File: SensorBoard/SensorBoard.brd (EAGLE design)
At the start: 134.6 x 100 mm, 70 parts, among them IC1 7805, J1 DCJ0202, U1 MPU-6000QFN-24, X1 gen1, X13 3.3out1, X14 3.3out2, X15 uart1, X16 uart2, X17 uart3, X18 uart4, X2 motordriver1, X3 MINI-USB-SCHIELD-32005-201, X4 gen2, X5 gen3, X6 gen4, X8 motordriver2

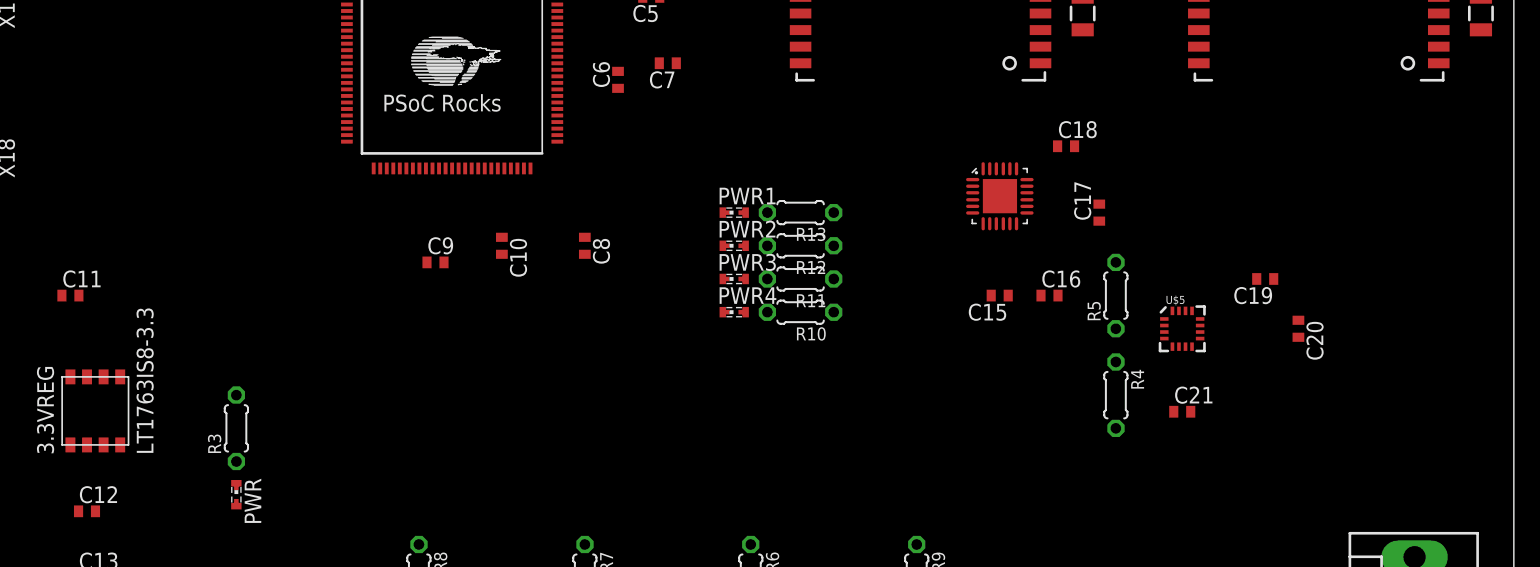
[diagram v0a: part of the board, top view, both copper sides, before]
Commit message: finished schematic.  All that is left is routing...
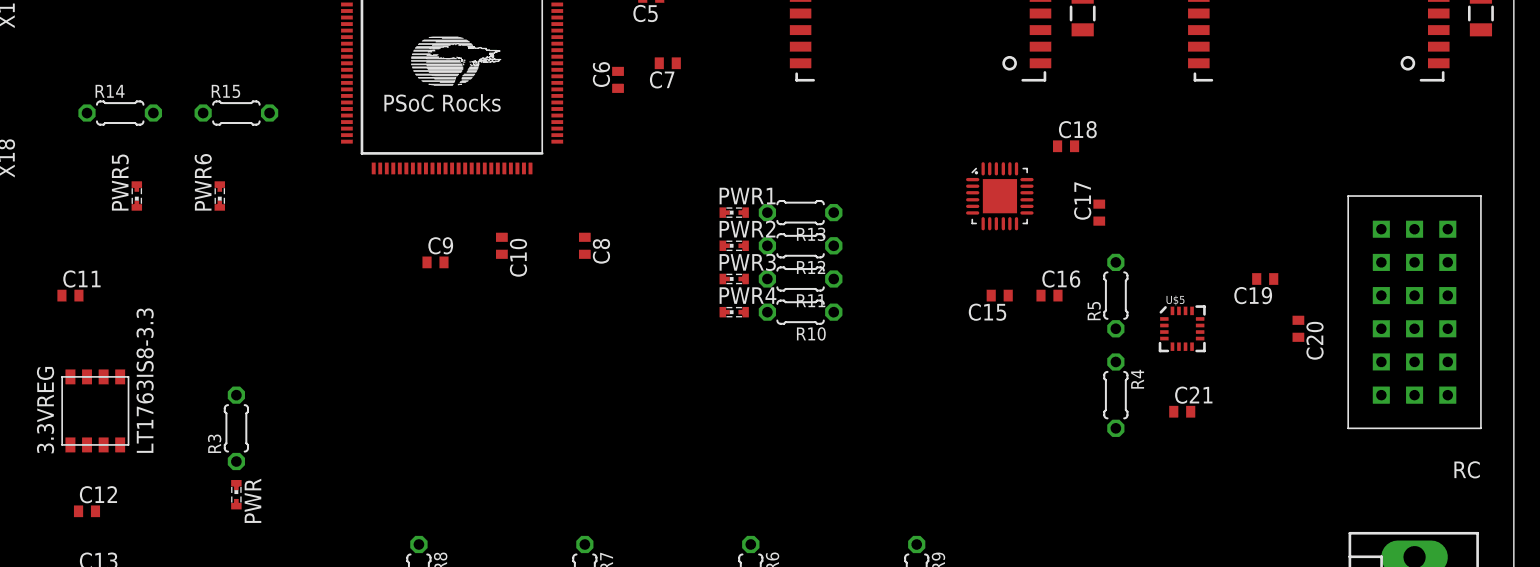
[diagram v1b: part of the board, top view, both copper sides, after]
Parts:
- added PWR5: GREEN, led:SMARTLED-TTW
- added PWR6: RED, led:SMARTLED-TTW
- added R14, R15: 4k, resistor:0204/5
- added RC: 6-CHANNEL, RCRECIEVER:6-CHANNEL
- C14: value 0.33uF -> 100nF
- X7: value (none) -> programmer
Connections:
- new net CH1: CY8C5868AXI-LP035.42, RC.P$3
- new net CH2: CY8C5868AXI-LP035.43, RC.P$6
- new net CH3: CY8C5868AXI-LP035.44, RC.P$9
- new net CH4: CY8C5868AXI-LP035.47, RC.P$12
- new net CH5: CY8C5868AXI-LP035.48, RC.P$15
- new net CH6: CY8C5868AXI-LP035.49, RC.P$18
- new net N$20: PWR5.A@1, R14.1
- new net N$21: PWR6.A@1, R15.1
- net +5V: now also RC.P$11, RC.P$14, RC.P$17, RC.P$2, RC.P$5, RC.P$8
- net CTS#: now also CY8C5868AXI-LP035.36
- net GND: now also PWR5.C@1, PWR6.C@1, RC.P$1, RC.P$10, RC.P$13, RC.P$16, RC.P$4, RC.P$7
- net RTS#: now also CY8C5868AXI-LP035.35
- net RXLED: now also R15.2
- net TXLED: now also R14.2
- net USB_RXD: now also CY8C5868AXI-LP035.27
- net USB_TXD: now also CY8C5868AXI-LP035.28

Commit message: fished SensorBoard.  It is perrrfect! - jack
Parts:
- removed U$5: HMC5883LSMD, SparkFun-Sensors:16LPCC
- removed U1: MPU-6000QFN-24, SparkFun-Sensors:QFN-24-TESTING
- removed X3: MINI-USB-SCHIELD-32005-201, con-cypressindustries:32005-201
- added ACC: MPU-6000QFN-24, SparkFun-Sensors:QFN-24-TESTING
- added MAGNETO: HMC5883LSMD, SparkFun-Sensors:16LPCC
- added MINIUSB: MINI-USB-SCHIELD-32005-201, con-cypressindustries:32005-201
- moved U$2 129.3 mm to (3.00, 92.0), turned to 0 degrees
- moved X15 112.2 mm to (122.0, 92.0), turned to 0 degrees
- moved X16 112.2 mm to (122.0, 80.0), turned to 0 degrees
- moved X17 112.1 mm to (122.0, 68.0), turned to 0 degrees
- moved X18 112.1 mm to (122.0, 56.0), turned to 0 degrees
- moved U$4 104.4 mm to (32.0, 92.0), turned to 0 degrees
- moved U$1 99.6 mm to (3.00, 70.0), turned to 0 degrees
- moved GPS2 87.0 mm to (25.0, 96.0), turned to 270 degrees
- moved C19 78.9 mm to (39.0, 23.0), turned to 0 degrees
- moved C20 77.4 mm to (42.0, 24.0)
- moved C14 77.3 mm to (100.0, 82.0), turned to 90 degrees
- moved USBUART 75.6 mm to (108.1, 77.9)
- moved R2 71.7 mm to (91.0, 83.0), turned to 0 degrees
- moved U$3 70.0 mm to (32.0, 70.0), turned to 0 degrees
- moved R1 69.7 mm to (97.0, 86.0), turned to 90 degrees
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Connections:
- new net +3.3VP1: PI.1
- new net +3.3VP2: PI.17
- new net +5VP1: PI.2
- new net +5VP2: PI.4
- new net 1: CY8C5868AXI-LP035.90
- new net 2: CY8C5868AXI-LP035.89
- new net 3: CY8C5868AXI-LP035.80
- new net 37: CY8C5868AXI-LP035.49
- new net 44: CY8C5868AXI-LP035.67
- net +3.3V: now also ACC.13, ACC.8, MAGNETO.13, MAGNETO.2, MAGNETO.4; no longer PI.1, PI.17, U$5.13, U$5.2, U$5.4, U1.13, U1.8
- net +5V: no longer PI.2, PI.4
- net AUXCL1: now also ACC.7, MAGNETO.1; no longer U$5.1, U1.7
- net AUXDA1: now also ACC.6, MAGNETO.16; no longer U$5.16, U1.6
- net CH1: now also CY8C5868AXI-LP035.51; no longer CY8C5868AXI-LP035.42
- net CH2: now also CY8C5868AXI-LP035.52; no longer CY8C5868AXI-LP035.43
- net CH3: now also CY8C5868AXI-LP035.53; no longer CY8C5868AXI-LP035.44
- net CH4: now also CY8C5868AXI-LP035.54; no longer CY8C5868AXI-LP035.47
- net CH5: now also CY8C5868AXI-LP035.55; no longer CY8C5868AXI-LP035.48
- net CH6: now also CY8C5868AXI-LP035.56; no longer CY8C5868AXI-LP035.49
- net CLKOUT1: now also ACC.22; no longer U1.22
- net CTS#: now also CY8C5868AXI-LP035.70; no longer CY8C5868AXI-LP035.36
- net D+: now also MINIUSB.3; no longer X3.3
- net D-: now also MINIUSB.2; no longer X3.2
- net FSYNC: now also ACC.11; no longer U1.11
- net GEN1: now also CY8C5868AXI-LP035.30; no longer CY8C5868AXI-LP035.31
- net GEN2: now also CY8C5868AXI-LP035.31; no longer CY8C5868AXI-LP035.32
- net GEN3: now also CY8C5868AXI-LP035.32; no longer CY8C5868AXI-LP035.33
- net GEN4: now also CY8C5868AXI-LP035.33; no longer CY8C5868AXI-LP035.34
- net GEN5: now also CY8C5868AXI-LP035.28; no longer CY8C5868AXI-LP035.29
- net GEN6: now also CY8C5868AXI-LP035.29; no longer CY8C5868AXI-LP035.30
- net GND: now also ACC.1, ACC.18, ACC.9, MAGNETO.11, MAGNETO.9, MINIUSB.1; no longer U$5.11, U$5.9, U1.1, U1.18, U1.9, X3.1
- net GPIO10: now also CY8C5868AXI-LP035.85; no longer CY8C5868AXI-LP035.82
- net GPIO11: now also CY8C5868AXI-LP035.83; no longer CY8C5868AXI-LP035.80
- net GPIO14: now also CY8C5868AXI-LP035.82; no longer CY8C5868AXI-LP035.1
- net GPIO15: now also CY8C5868AXI-LP035.81; no longer CY8C5868AXI-LP035.2
- net GPIO17: now also CY8C5868AXI-LP035.91; no longer CY8C5868AXI-LP035.85
- net GPIO18: no longer CY8C5868AXI-LP035.3
- net GPIO2(0): now also CY8C5868AXI-LP035.94; no longer CY8C5868AXI-LP035.91
- net GPIO22: no longer CY8C5868AXI-LP035.83
- net GPIO23: now also CY8C5868AXI-LP035.79; no longer CY8C5868AXI-LP035.16
- net GPIO24: now also CY8C5868AXI-LP035.78; no longer CY8C5868AXI-LP035.17
- net GPIO25: no longer CY8C5868AXI-LP035.18
- net GPIO27: no longer CY8C5868AXI-LP035.84
- net GPIO3(1): now also CY8C5868AXI-LP035.93; no longer CY8C5868AXI-LP035.90
- net GPIO4: now also CY8C5868AXI-LP035.92; no longer CY8C5868AXI-LP035.89
- net GPIO7: no longer CY8C5868AXI-LP035.52
- net GPIO8: no longer CY8C5868AXI-LP035.19
- net GPIO9: now also CY8C5868AXI-LP035.84; no longer CY8C5868AXI-LP035.81
- net GPS1RXA: now also CY8C5868AXI-LP035.19; no longer CY8C5868AXI-LP035.7
- net GPS1RXB: now also CY8C5868AXI-LP035.22; no longer CY8C5868AXI-LP035.9
- net GPS1TXA: now also CY8C5868AXI-LP035.17; no longer CY8C5868AXI-LP035.6
- net GPS1TXB: now also CY8C5868AXI-LP035.18; no longer CY8C5868AXI-LP035.8
- net GPS1XSTB: now also CY8C5868AXI-LP035.23; no longer CY8C5868AXI-LP035.22
- net GPS2RXA: now also CY8C5868AXI-LP035.3; no longer CY8C5868AXI-LP035.98
- net GPS2RXB: now also CY8C5868AXI-LP035.4; no longer CY8C5868AXI-LP035.96
- net GPS2TXA: now also CY8C5868AXI-LP035.1; no longer CY8C5868AXI-LP035.99
- net GPS2TXB: now also CY8C5868AXI-LP035.2; no longer CY8C5868AXI-LP035.97
- net GPS2XSTB: now also CY8C5868AXI-LP035.5; no longer CY8C5868AXI-LP035.23
- net GPS3RXA: now also CY8C5868AXI-LP035.8; no longer CY8C5868AXI-LP035.94
- net GPS3RXB: now also CY8C5868AXI-LP035.9; no longer CY8C5868AXI-LP035.92
- net GPS3TXA: now also CY8C5868AXI-LP035.6; no longer CY8C5868AXI-LP035.95
- net GPS3TXB: now also CY8C5868AXI-LP035.7; no longer CY8C5868AXI-LP035.93
- net GPS3XSTB: now also CY8C5868AXI-LP035.16; no longer CY8C5868AXI-LP035.24
- net GPS4RXA: now also CY8C5868AXI-LP035.97; no longer CY8C5868AXI-LP035.78
- net GPS4RXB: now also CY8C5868AXI-LP035.98; no longer CY8C5868AXI-LP035.76
- net GPS4TXA: now also CY8C5868AXI-LP035.95; no longer CY8C5868AXI-LP035.79
- net GPS4TXB: now also CY8C5868AXI-LP035.96; no longer CY8C5868AXI-LP035.77
- net GPS4XSTB: now also CY8C5868AXI-LP035.99; no longer CY8C5868AXI-LP035.25
- net INT1: now also ACC.12, CY8C5868AXI-LP035.27; no longer U1.12
- net MDTX1: now also CY8C5868AXI-LP035.34; no longer CY8C5868AXI-LP035.46
- net MDTX2: now also CY8C5868AXI-LP035.35; no longer CY8C5868AXI-LP035.45
- net N$11: now also MAGNETO.12; no longer U$5.12
- net N$15: now also MAGNETO.8; no longer U$5.8
- net N$16: now also MAGNETO.10; no longer U$5.10
- net N$6: now also MINIUSB.4, MINIUSB.5; no longer X3.4, X3.5
- net N$7: now also ACC.10; no longer U1.10
- net N$8: now also ACC.20; no longer U1.20
- net PWREN#: now also CY8C5868AXI-LP035.74
- net RTS#: now also CY8C5868AXI-LP035.71; no longer CY8C5868AXI-LP035.35
- net RX1: now also CY8C5868AXI-LP035.77; no longer CY8C5868AXI-LP035.74
- net RX2: now also CY8C5868AXI-LP035.69; no longer CY8C5868AXI-LP035.72
- net RX3: now also CY8C5868AXI-LP035.48; no longer CY8C5868AXI-LP035.70
- net RX4: now also CY8C5868AXI-LP035.46; no longer CY8C5868AXI-LP035.68
- net SCL_ACC: now also ACC.23, CY8C5868AXI-LP035.25; no longer CY8C5868AXI-LP035.4, U1.23
- net SDA_ACC: now also ACC.24, CY8C5868AXI-LP035.24; no longer CY8C5868AXI-LP035.5, U1.24
- net STATUS1: now also CY8C5868AXI-LP035.44; no longer CY8C5868AXI-LP035.56
- net STATUS2: now also CY8C5868AXI-LP035.43; no longer CY8C5868AXI-LP035.55
- net STATUS3: now also CY8C5868AXI-LP035.42; no longer CY8C5868AXI-LP035.54
- net STATUS4: now also CY8C5868AXI-LP035.36; no longer CY8C5868AXI-LP035.53
- net TX1: now also CY8C5868AXI-LP035.76; no longer CY8C5868AXI-LP035.73
- net TX2: now also CY8C5868AXI-LP035.68; no longer CY8C5868AXI-LP035.71
- net TX3: now also CY8C5868AXI-LP035.47; no longer CY8C5868AXI-LP035.69
- net TX4: now also CY8C5868AXI-LP035.45; no longer CY8C5868AXI-LP035.67
- net USB_RXD: now also CY8C5868AXI-LP035.73; no longer CY8C5868AXI-LP035.27
- net USB_TXD: now also CY8C5868AXI-LP035.72; no longer CY8C5868AXI-LP035.28
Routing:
- net +5V: track 0.00 -> 475.9 mm, vias 0 -> 5
- net GND: track 0.00 -> 371.4 mm, vias 0 -> 18
- net +3.3V: track 0.00 -> 247.9 mm, vias 0 -> 4
- net XRES: track 0.00 -> 101.4 mm, vias 0 -> 2
- net SCLK: track 0.00 -> 89.9 mm
- net SDAT: track 0.00 -> 86.3 mm, vias 0 -> 2
- net MDTX2: track 0.00 -> 71.3 mm, vias 0 -> 2
- net GEN5: track 0.00 -> 64.4 mm, vias 0 -> 2
- net MDTX1: track 0.00 -> 62.4 mm, vias 0 -> 2
- net TX3: track 0.00 -> 61.6 mm, vias 0 -> 1
- net GPS2TXA: track 0.00 -> 61.0 mm, vias 0 -> 2
- net GPS2TXB: track 0.00 -> 60.0 mm, vias 0 -> 2
- net GPS2RXA: track 0.00 -> 58.9 mm, vias 0 -> 2
- net GPS2RXB: track 0.00 -> 57.6 mm, vias 0 -> 2
- net GPS1RXB: track 0.00 -> 56.9 mm, vias 0 -> 2
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- added copper zone on layer 1, net GND
- added copper zone on layer 16, net GND
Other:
- board size 134.6 x 100 mm -> 136.2 x 101 mm

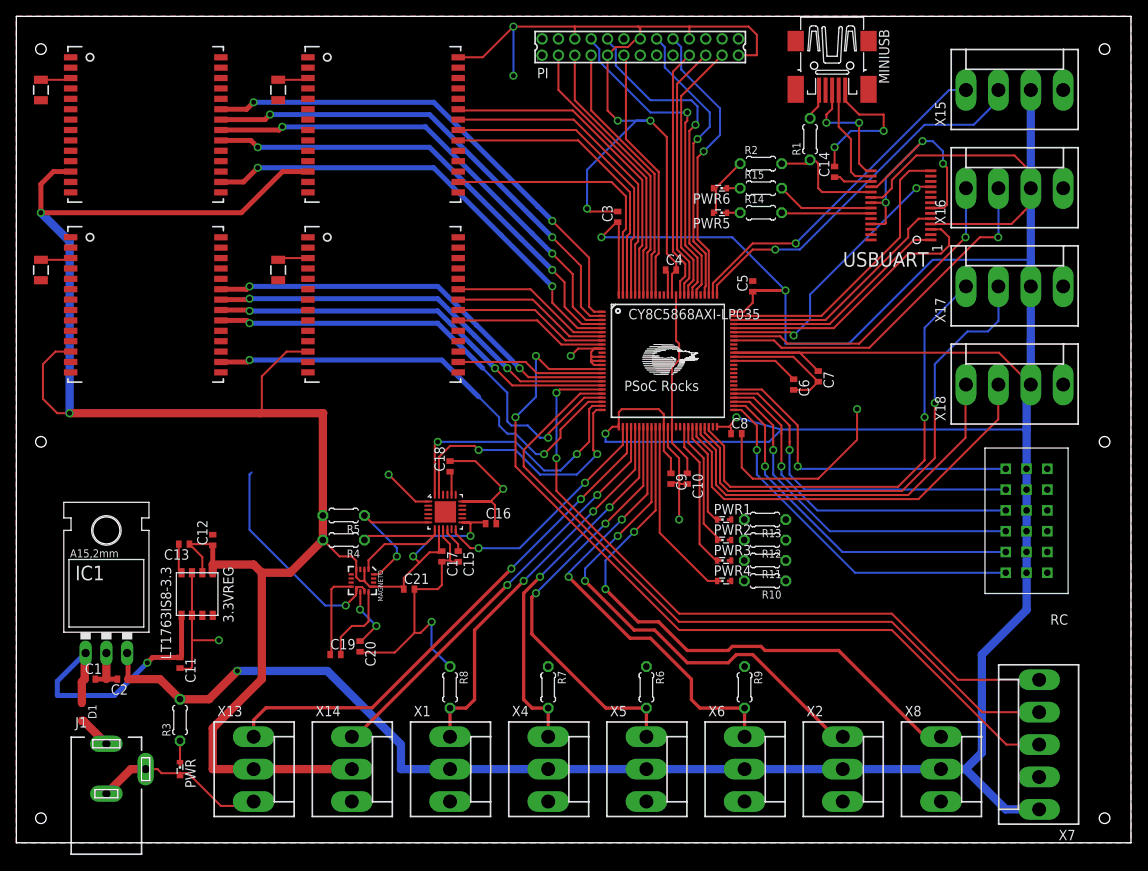
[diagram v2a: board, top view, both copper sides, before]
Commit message: added screw holes
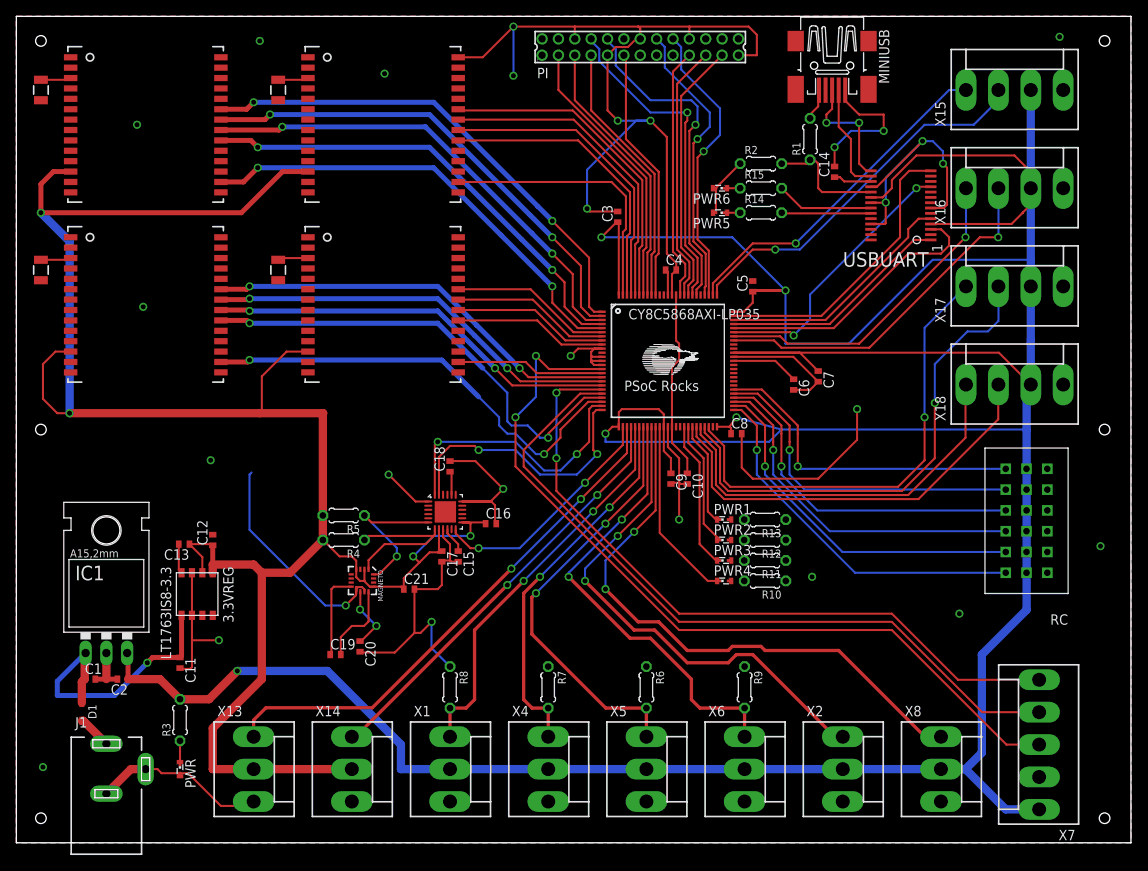
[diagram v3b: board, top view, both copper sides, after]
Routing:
- net GND: vias 18 -> 28
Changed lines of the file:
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@@
 <setting verticaltext="up"/>
 </settings>
-<grid distance="0.25" unitdist="mm" unit="mm" style="lines" multiple="1" display="yes" altdistance="0.025" altunitdist="inch" altunit="inch"/>
+<grid distance="1" unitdist="mm" unit="mm" style="lines" multiple="1" display="yes" altdistance="0.025" altunitdist="inch" altunit="inch"/>
 <layers>
 <layer number="1" name="Top" color="4" fill="1" visible="yes" active="yes"/>
@@
 <wire x1="0" y1="101" x2="0" y2="0" width="0" layer="20"/>
 <hole x="3" y="3" drill="1.3"/>
-<hole x="3" y="97" drill="1.3"/>
-<hole x="133" y="97" drill="1.3"/>
+<hole x="3" y="98" drill="1.3"/>
+<hole x="133" y="98" drill="1.3"/>
 <hole x="133" y="3" drill="1.3"/>
-<hole x="133" y="49" drill="1.3"/>
-<hole x="3" y="49" drill="1.3"/>
+<hole x="133" y="50.5" drill="1.3"/>
+<hole x="3" y="50.5" drill="1.3"/>
 </plain>
 <attributes>
@@
 <vertex x="0" y="0"/>
 </polygon>
+<wire x1="85.5" y1="77" x2="85.5" y2="80" width="0.254" layer="1"/>
+<wire x1="85.5" y1="80" x2="85.5" y2="80.04" width="0.254" layer="1"/>
+<wire x1="85.5" y1="80.04" x2="88.46" y2="83" width="0.254" layer="1"/>
+<via x="23.75" y="46.75" extent="1-16" drill="0.6" shape="square"/>
+<via x="3.25" y="9.25" extent="1-16" drill="0.6" shape="square"/>
+<via x="97.25" y="32.5" extent="1-16" drill="0.6" shape="square"/>
+<via x="115.25" y="28" extent="1-16" drill="0.6" shape="square"/>
+<via x="132.5" y="36.25" extent="1-16" drill="0.6" shape="square"/>
+<via x="29.75" y="98" extent="1-16" drill="0.6" shape="square"/>
+<via x="14.75" y="87.75" extent="1-16" drill="0.6" shape="square"/>
+<via x="15.5" y="65.5" extent="1-16" drill="0.6" shape="square"/>
+<via x="45" y="94" extent="1-16" drill="0.6" shape="square"/>
+<via x="127.5" y="98.5" extent="1-16" drill="0.6" shape="square"/>
 <wire x1="104.444" y1="75.625" x2="104.444" y2="74.975" width="0" layer="19" extent="1-1"/>
 <wire x1="87.676" y1="60.396" x2="87.676" y2="59.396" width="0" layer="19" extent="1-1"/>
@@
 <wire x1="6.6358" y1="88.38" x2="6.6358" y2="92.19" width="0" layer="19" extent="1-1"/>
 <wire x1="6.6358" y1="66.38" x2="6.6358" y2="70.19" width="0" layer="19" extent="1-1"/>
-<wire x1="85.5" y1="77" x2="85.5" y2="80" width="0.254" layer="1"/>
-<wire x1="85.5" y1="80" x2="85.5" y2="80.04" width="0.254" layer="1"/>
-<wire x1="85.5" y1="80.04" x2="88.46" y2="83" width="0.254" layer="1"/>
 </signal>
 <signal name="+12V">
@@
 </signal>
 </signals>
-<errors>
-</errors>
 </board>
 </drawing>

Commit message: made drill holes larger for the rc
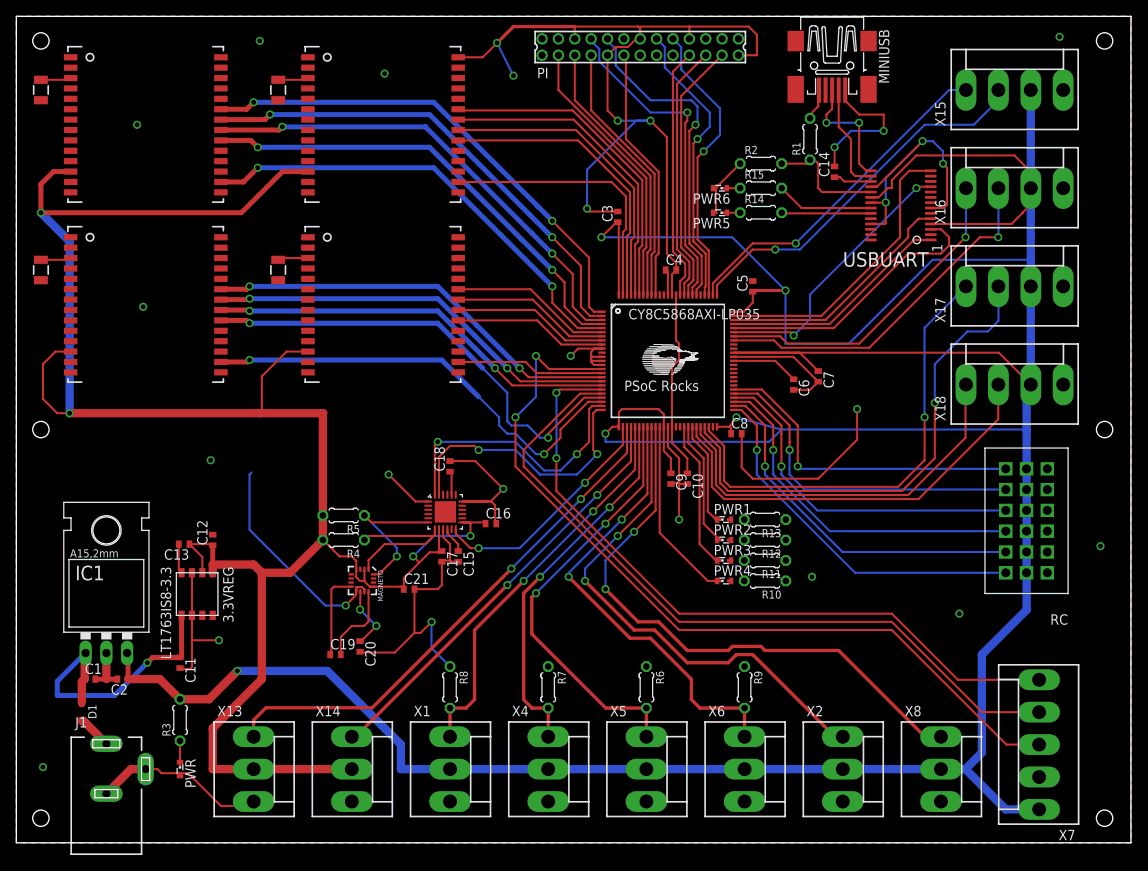
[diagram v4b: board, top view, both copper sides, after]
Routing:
- net GND: track 371.4 -> 369.5 mm
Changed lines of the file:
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@@
 <wire x1="136.22" y1="101" x2="0" y2="101" width="0" layer="20"/>
 <wire x1="0" y1="101" x2="0" y2="0" width="0" layer="20"/>
-<hole x="3" y="3" drill="1.3"/>
-<hole x="3" y="98" drill="1.3"/>
-<hole x="133" y="98" drill="1.3"/>
-<hole x="133" y="3" drill="1.3"/>
-<hole x="133" y="50.5" drill="1.3"/>
-<hole x="3" y="50.5" drill="1.3"/>
+<hole x="3" y="3" drill="2"/>
+<hole x="3" y="98" drill="2"/>
+<hole x="133" y="98" drill="2"/>
+<hole x="133" y="3" drill="2"/>
+<hole x="133" y="50.5" drill="2"/>
+<hole x="3" y="50.5" drill="2"/>
 </plain>
 <attributes>
@@
 <wire x1="73.25" y1="97.25" x2="72.25" y2="96.25" width="0.254" layer="1"/>
 <wire x1="54" y1="96" x2="57" y2="96" width="0.254" layer="1"/>
-<wire x1="57" y1="96" x2="60.75" y2="99.75" width="0.254" layer="1"/>
-<via x="60.75" y="99.75" extent="1-16" drill="0.6" shape="square"/>
-<wire x1="60.75" y1="99.75" x2="60.75" y2="93.75" width="0.254" layer="16"/>
+<wire x1="57" y1="96" x2="58.75" y2="97.75" width="0.254" layer="1"/>
+<via x="58.75" y="97.75" extent="1-16" drill="0.6" shape="square"/>
+<wire x1="58.75" y1="97.75" x2="60.75" y2="93.75" width="0.254" layer="16"/>
 <via x="60.75" y="93.75" extent="1-16" drill="0.6" shape="square"/>
-<wire x1="60.75" y1="99.75" x2="68.25" y2="99.75" width="0.254" layer="1"/>
 <wire x1="72.25" y1="96.25" x2="72.25" y2="89.5" width="0.254" layer="1"/>
 <wire x1="72.25" y1="89.5" x2="73.5" y2="88.25" width="0.254" layer="1"/>
@@
 <via x="45" y="94" extent="1-16" drill="0.6" shape="square"/>
 <via x="127.5" y="98.5" extent="1-16" drill="0.6" shape="square"/>
+<wire x1="68.25" y1="99.75" x2="60.75" y2="99.75" width="0.4064" layer="1"/>
+<wire x1="60.75" y1="99.75" x2="59" y2="98" width="0.4064" layer="1"/>
 <wire x1="104.444" y1="75.625" x2="104.444" y2="74.975" width="0" layer="19" extent="1-1"/>
 <wire x1="87.676" y1="60.396" x2="87.676" y2="59.396" width="0" layer="19" extent="1-1"/>
@@
 <wire x1="38" y1="21" x2="47" y2="12" width="1.016" layer="16"/>
 <wire x1="47" y1="12" x2="47" y2="9" width="1.016" layer="16"/>
-<wire x1="104.444" y1="78.875" x2="105.875" y2="78.875" width="0.254" layer="1"/>
-<wire x1="105.875" y1="78.875" x2="107" y2="80" width="0.254" layer="1"/>
 <wire x1="107" y1="80" x2="107" y2="81" width="0.254" layer="1"/>
 <wire x1="107" y1="81" x2="110" y2="84" width="0.254" layer="1"/>
@@
 <wire x1="101.75" y1="61" x2="112" y2="71.25" width="0.254" layer="16"/>
 <wire x1="112" y1="71.25" x2="123.98" y2="71.25" width="0.254" layer="16"/>
+<wire x1="107" y1="80" x2="106.5" y2="80" width="0.254" layer="1"/>
+<wire x1="106.5" y1="80" x2="105.375" y2="78.875" width="0.254" layer="1"/>
+<wire x1="104.444" y1="78.875" x2="105.375" y2="78.875" width="0.254" layer="1"/>
 <wire x1="73.626" y1="66.946" x2="79.626" y2="66.946" width="0" layer="19" extent="1-1"/>
 </signal>

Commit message: most recent version of the board
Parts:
- removed D1: (no value), zetex:SOD323
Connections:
- removed net N$3: D1.2, J1.1
- net +12V: now also J1.1; no longer D1.1
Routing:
- net +12V: track 35.1 -> 42.1 mm
- net N$3: track 4.16 -> 0.00 mm
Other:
- board text added: "1"
- board text added: "A15,2mm"
- board text added: "PSoC Rocks"
- board text added: "Quadcopter Sensor Board V1.0"
